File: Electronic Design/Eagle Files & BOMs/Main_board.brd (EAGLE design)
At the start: 100 x 64 mm, 49 parts, among them IC2 ATMEGA328-PU, IC3 LM2576S, Q1 IRF9540, Q2 IRF9540, X1 16MHz

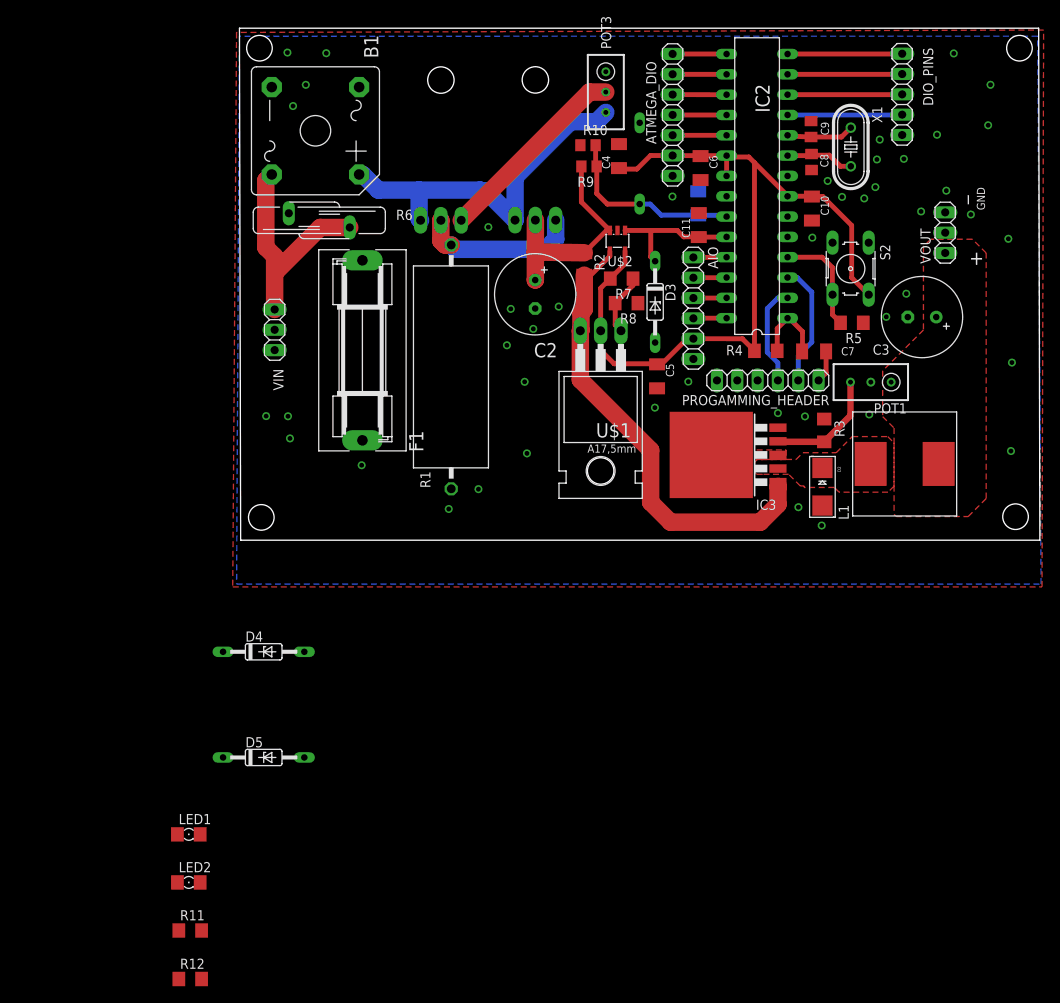
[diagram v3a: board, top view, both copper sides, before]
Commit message: Adding new overvoltage protection FETs and renaming nets
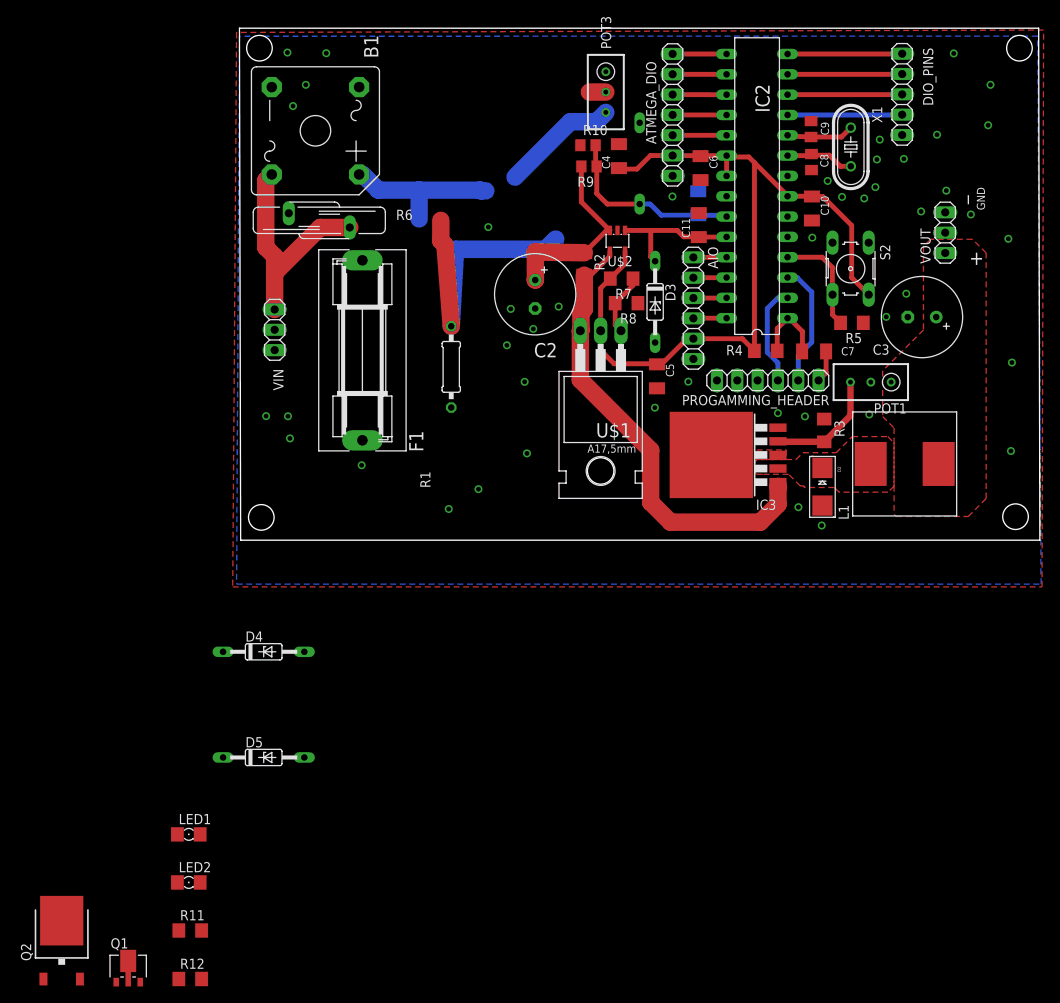
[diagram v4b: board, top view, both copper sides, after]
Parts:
- Q1: value IRF9540 -> BSS192P; device transistor-power:TO220BH -> Samson:BSS192P
- Q2: value IRF9540 -> FQD7P20; device transistor-power:TO220BH -> Samson:TO252
- R1: value 1k -> 100k; device resistor:VTA52 -> resistor:0207/10
- moved Q2 113.1 mm to (-22.2, -45.1), flipped to the top
- moved Q1 107.2 mm to (-13.9, -48.5), flipped to the top
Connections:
- net M1S renamed VIN_CURRENT_MEASURED
- net N$1 renamed VIN_AC1
- net N$11 renamed D11
- net N$12 renamed D12
- net N$13 renamed BUCK_OUTPUT
- net N$15 renamed CRYSTAL2
- net N$16 renamed CRYSTAL1
- net N$17 renamed RESET
- net N$19 renamed VIN_AC2
- net N$2 renamed VOUT_PREFUSE
- net N$20 renamed D8
- net N$21 renamed D7
- net N$22 renamed D6
- net N$24 renamed VOUT_FINAL
- net N$25 renamed D5
- net N$26 renamed BUCK_FEEDBACK
- net N$6 renamed D9
- net N$8 renamed D13
- net N$9 renamed D10
- removed net N$10: B1.+, POT3.3, Q1.S, Q2.S
- removed net N$3: C2.+, Q2.D, R2.1, R9.2, U$2.3
- removed net N$35: Q1.D, Q2.G, R1.2
- removed net N$7: POT3.2, Q1.G
- new net Q1_GATE: POT3.2, Q1.1
- new net Q2_GATE: Q1.2, Q1.4, Q2.1, R1.2
- new net VIN_PROTECTED: C2.+, Q2.3, R2.1, R9.2, U$2.3
- new net VIN_UNPROTECTED: B1.+, POT3.3, Q1.3, Q2.2
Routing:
- net N$10: track 45.8 -> 0.00 mm
- net Q2_GATE: track 0.00 -> 36.2 mm
- net VIN_UNPROTECTED: track 0.00 -> 35.0 mm
- net N$3: track 27.4 -> 0.00 mm
- net N$7: track 24.7 -> 0.00 mm
- net VIN_PROTECTED: track 0.00 -> 23.5 mm
- net N$35: track 20.3 -> 0.00 mm
- net Q1_GATE: track 0.00 -> 2.05 mm

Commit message: Moving everything into postion and adding fuse to start of circuit
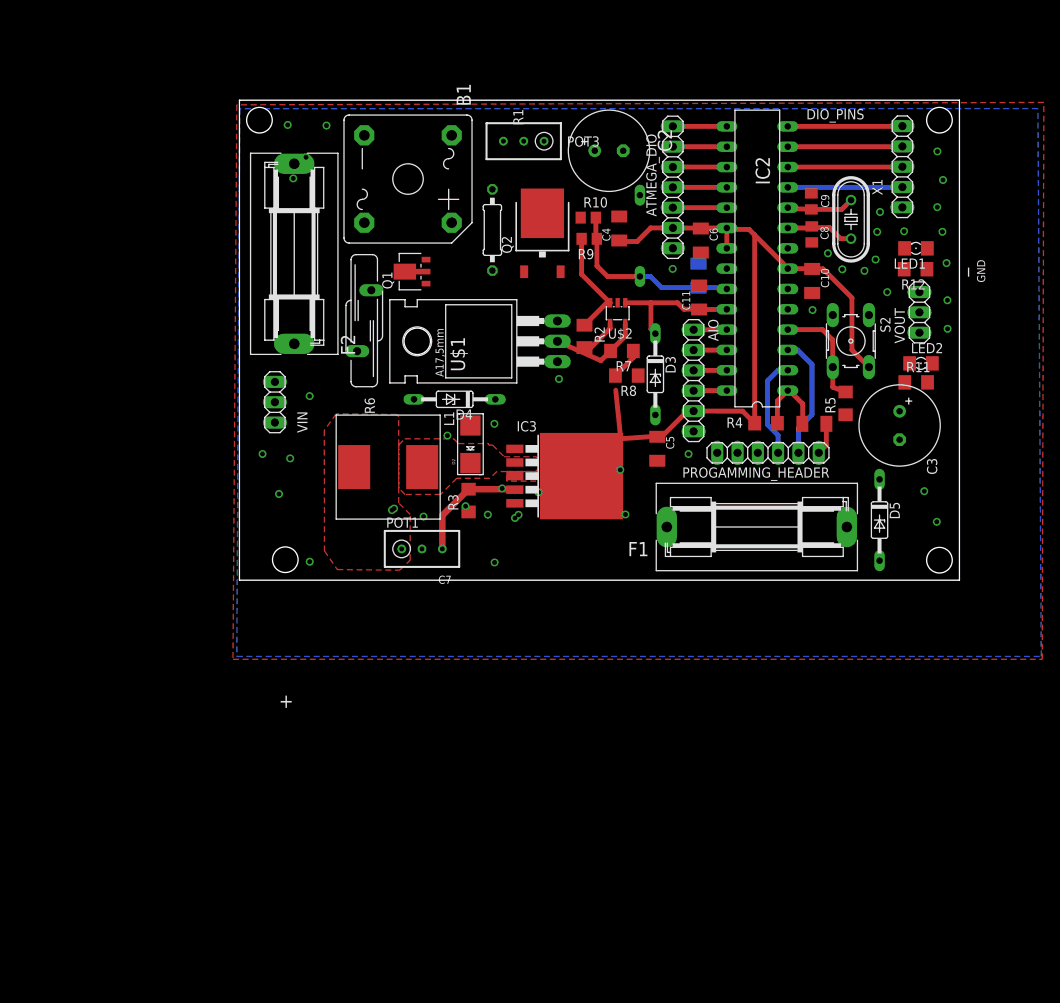
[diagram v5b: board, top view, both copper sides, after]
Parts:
- added F2: FUSESH22,5A, fuse:SH22,5A
- moved R12 126.9 mm to (84.5, 38.9), turned to 180 degrees
- moved LED1 116.7 mm to (84.6, 41.5), turned to 180 degrees
- moved R11 113.7 mm to (84.6, 24.7)
- moved LED2 112.2 mm to (85.2, 27.1)
- moved Q2 106.9 mm to (37.9, 43.4)
- moved Q1 94.0 mm to (21.6, 38.6), turned to 90 degrees
- moved D5 82.5 mm to (80.0, 7.52), turned to 270 degrees
- moved L1 64.6 mm to (18.6, 14.1), turned to 270 degrees
- moved POT1 59.8 mm to (22.8, 3.91), turned to 270 degrees
- moved F1 54.0 mm to (64.7, 6.65), turned to 0 degrees
- moved R3 45.3 mm to (28.6, 9.95), turned to 90 degrees
- moved D2 44.3 mm to (28.9, 17.0), turned to 90 degrees
- moved D4 39.6 mm to (26.9, 22.6), turned to 180 degrees
- moved IC3 21.5 mm to (40.2, 13.0), turned to 270 degrees
- moved C2 20.2 mm to (46.2, 53.7), turned to 0 degrees
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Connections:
- new net N$1: F2.1, VIN.3
- net VIN_AC1: now also F2.2; no longer VIN.3
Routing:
- net VIN_CURRENT_MEASURED: track 57.9 -> 4.98 mm
- net Q2_GATE: track 36.2 -> 0.00 mm
- net VIN_UNPROTECTED: track 35.0 -> 0.00 mm
- net VIN_AC2: track 29.4 -> 0.00 mm
- net VIN_PROTECTED: track 23.5 -> 13.8 mm
- net N$23: track 7.74 -> 4.00 mm
- net Q1_GATE: track 2.05 -> 0.00 mm
- net +5V: track 104.8 -> 105.9 mm
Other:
- board size 100 x 64 mm -> 90 x 60 mm

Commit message: moving everything into place and DRC check complete
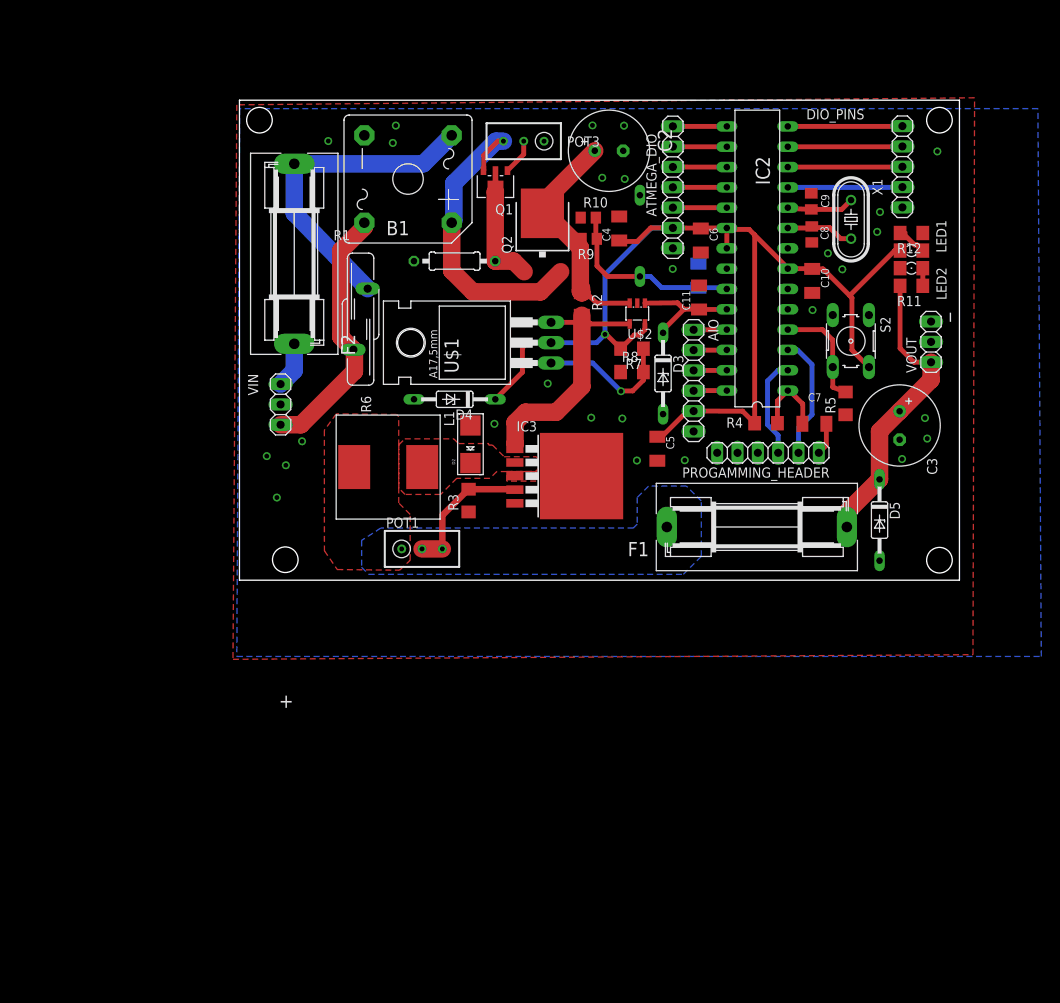
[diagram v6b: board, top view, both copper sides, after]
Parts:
- moved Q1 15.1 mm to (32.0, 49.5), turned to 180 degrees
- moved R11 12.1 mm to (84.0, 36.8), turned to 180 degrees
- moved LED2 12.0 mm to (84.0, 39.0), turned to 180 degrees
- moved R1 6.12 mm to (26.9, 39.9), turned to 0 degrees
- moved R12 4.56 mm to (84.0, 43.4)
- moved R2 4.05 mm to (42.8, 34.5)
- moved VOUT 3.96 mm to (86.5, 29.8)
- moved U$2 2.45 mm to (49.7, 33.3)
- moved R7 1.29 mm to (49.1, 28.9)
- moved D3 0.97 mm to (53.0, 25.8)
- moved U$1 0.82 mm to (32.6, 29.7)
- moved R8 0.78 mm to (49.1, 26.0), turned to 0 degrees
- moved VIN 0.76 mm to (5.14, 22.0), turned to 90 degrees
- moved LED1 0.63 mm to (84.0, 41.2), turned to 0 degrees
- moved R6 0.50 mm to (15.1, 32.6)
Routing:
- net VIN_AC1: track 0.00 -> 40.5 mm
- net VIN_UNPROTECTED: track 0.00 -> 40.3 mm
- net VOUT_FINAL: track 0.00 -> 37.4 mm
- net VIN_AC2: track 0.00 -> 32.5 mm
- net +5V: track 105.9 -> 136.9 mm, vias 0 -> 1
- net VIN_CURRENT_MEASURED: track 4.98 -> 33.1 mm
- net VIN_PROTECTED: track 13.8 -> 31.3 mm
- net N$23: track 4.00 -> 17.9 mm, vias 0 -> 1
- net Q2_GATE: track 0.00 -> 12.8 mm
- net N$1: track 0.00 -> 5.75 mm
- net Q1_GATE: track 0.00 -> 4.52 mm
- net N$28: track 0.00 -> 4.40 mm
- net BUCK_FEEDBACK: track 14.6 -> 17.2 mm
- net IIN: track 17.2 -> 14.7 mm
- net N$18: track 0.00 -> 2.20 mm
- added copper zone on layer 1, net VOUT_PREFUSE
- added copper zone on layer 16, net VOUT_PREFUSE
- removed copper zone on layer 1, net VOUT_FINAL
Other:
- board text removed: "GND"

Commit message: Moving buck converter and re-arranging other components as needed
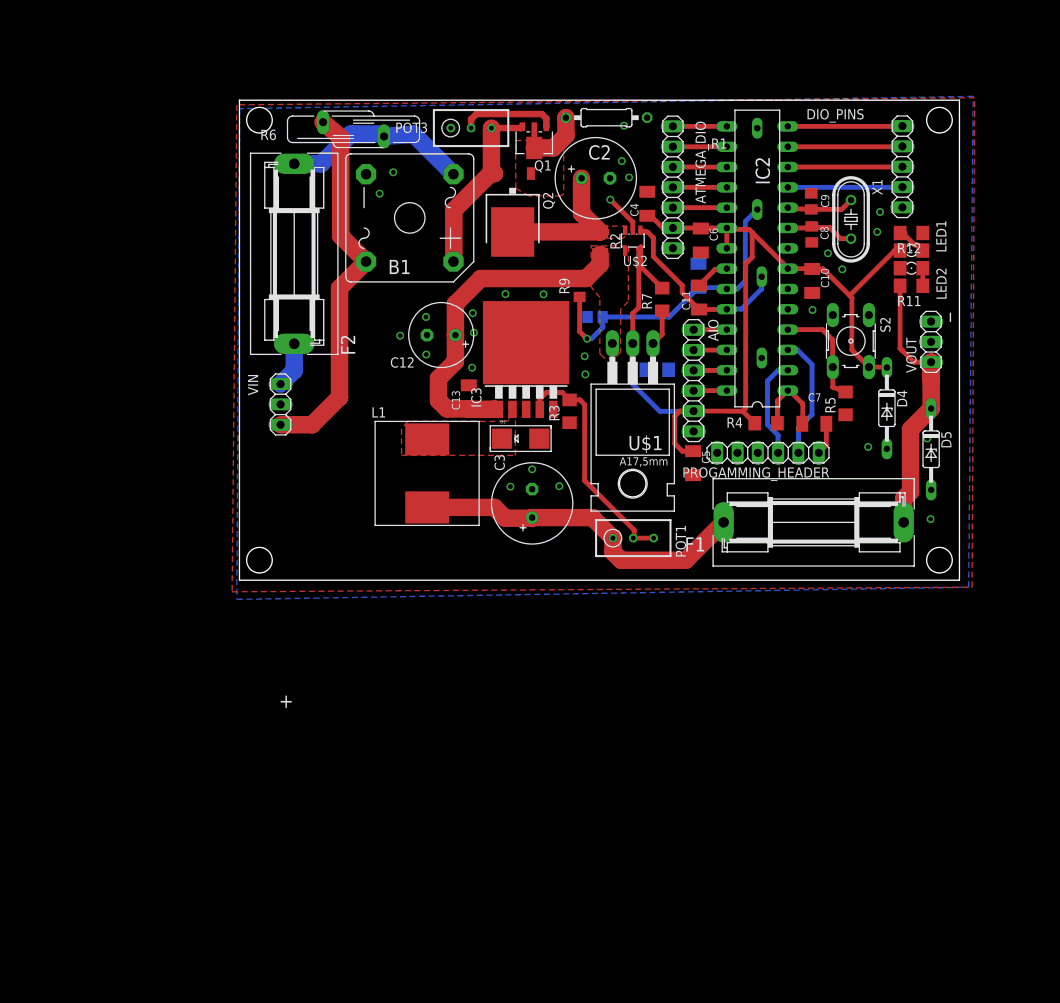
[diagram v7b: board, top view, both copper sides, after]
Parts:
- added C12: 100uF, resistor:E3,5-8
- added C13: 0.1u, resistor:C1206K
- moved D4 54.0 mm to (80.9, 21.5), turned to 270 degrees
- moved C3 47.0 mm to (36.6, 9.60), turned to 90 degrees
- moved POT1 26.4 mm to (49.2, 5.26)
- moved R1 26.1 mm to (45.9, 57.8), turned to 180 degrees
- moved R6 23.7 mm to (14.3, 56.4), turned to 90 degrees
- moved U$1 17.8 mm to (49.2, 23.2), turned to 180 degrees
- moved D1 16.9 mm to (64.7, 51.4)
- moved R3 16.9 mm to (41.3, 21.1)
- moved IC3 14.8 mm to (35.8, 27.1), turned to 0 degrees
- moved D3 14.2 mm to (65.3, 32.9), flipped to the bottom
- moved R10 12.4 mm to (44.5, 32.9), flipped to the bottom, turned to 180 degrees
- moved D5 11.0 mm to (86.5, 16.4)
- moved U$2 9.14 mm to (49.2, 42.5)
- moved R2 7.95 mm to (45.1, 42.1)
- moved Q1 7.32 mm to (36.9, 54.9)
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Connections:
- net GND: now also C12.-, C13.2, IC3.6
- net VIN_CURRENT_MEASURED: now also C12.+, C13.1, R9.2
- net VIN_PROTECTED: no longer R9.2
- net VOUT_FINAL: no longer C3.+
- net VOUT_PREFUSE: now also C3.+
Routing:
- net VOUT_PREFUSE: track 0.00 -> 42.8 mm
- net VIN_UNPROTECTED: track 40.3 -> 23.2 mm
- net VIN_AC1: track 40.5 -> 23.8 mm
- net VIN: track 23.5 -> 38.9 mm, vias 0 -> 1
- net VIN_AC2: track 32.5 -> 46.9 mm
- net VIN_PROTECTED: track 31.3 -> 18.6 mm
- net BUCK_FEEDBACK: track 17.2 -> 29.7 mm
- net VIN_CURRENT_MEASURED: track 33.1 -> 43.4 mm
- net N$23: track 17.9 -> 8.21 mm, vias 1 -> 0
- net GND: track 0.00 -> 9.32 mm
- net IIN: track 14.7 -> 23.7 mm
- net +5V: track 136.9 -> 128.9 mm, vias 1 -> 0
- net Q1_GATE: track 4.52 -> 12.0 mm
- net Q2_GATE: track 12.8 -> 9.18 mm
- net VOUT_FINAL: track 37.4 -> 36.4 mm
- added copper zone on layer 1, net Q2_GATE
- added copper zone on layer 1, net VIN_CURRENT_MEASURED
- added copper zone on layer 1, net VIN_PROTECTED
- removed copper zone on layer 1, net VOUT_PREFUSE
- removed copper zone on layer 16, net VOUT_PREFUSE
